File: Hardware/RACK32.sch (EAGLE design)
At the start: 95 parts, among them IC1 MCP9808-MSOP8, IC2 ESPWROOM32, IC3 LM358D, IC4 W5500-LQFP, IC5 CP2102N-A01-GQFN24, J1 SPI-LCD, J10 microSD, J11 IO, J2 I2CBR, J3 USB-C-16P-16P, J4 DC IN, J6 PWR_LED, Q1 FDN340P, Q2 MMDT3904, U1 HY931147C-RJ45

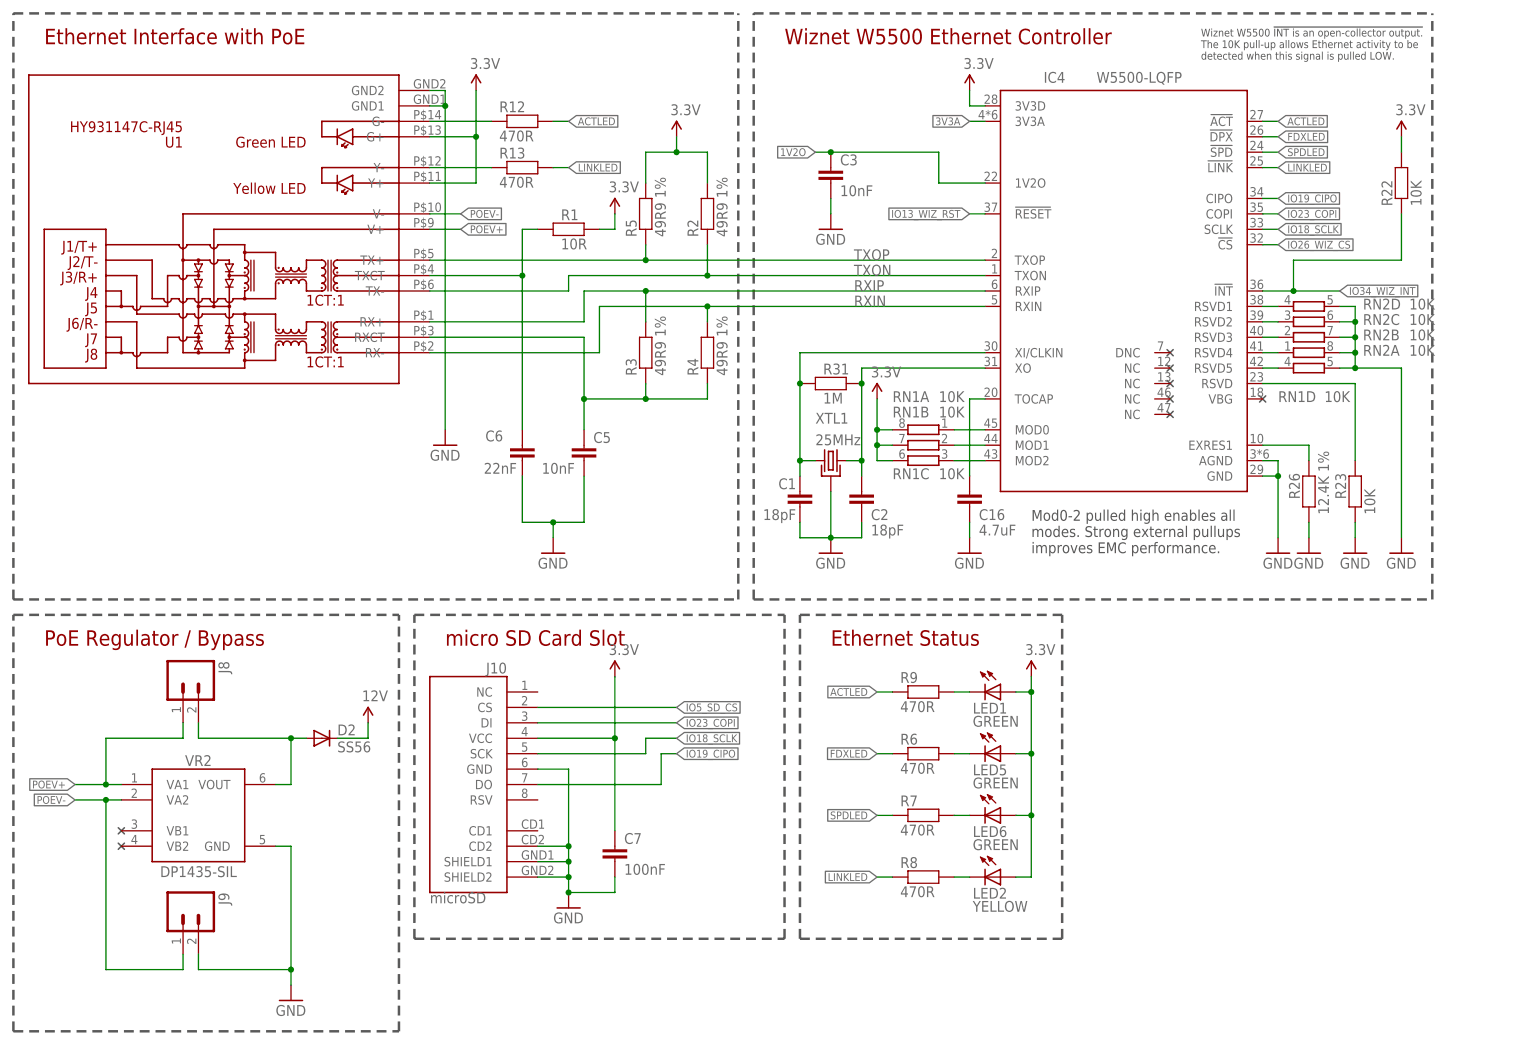
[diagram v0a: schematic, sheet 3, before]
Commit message: Changed PTC to 1206 size. Replaced power LED header.
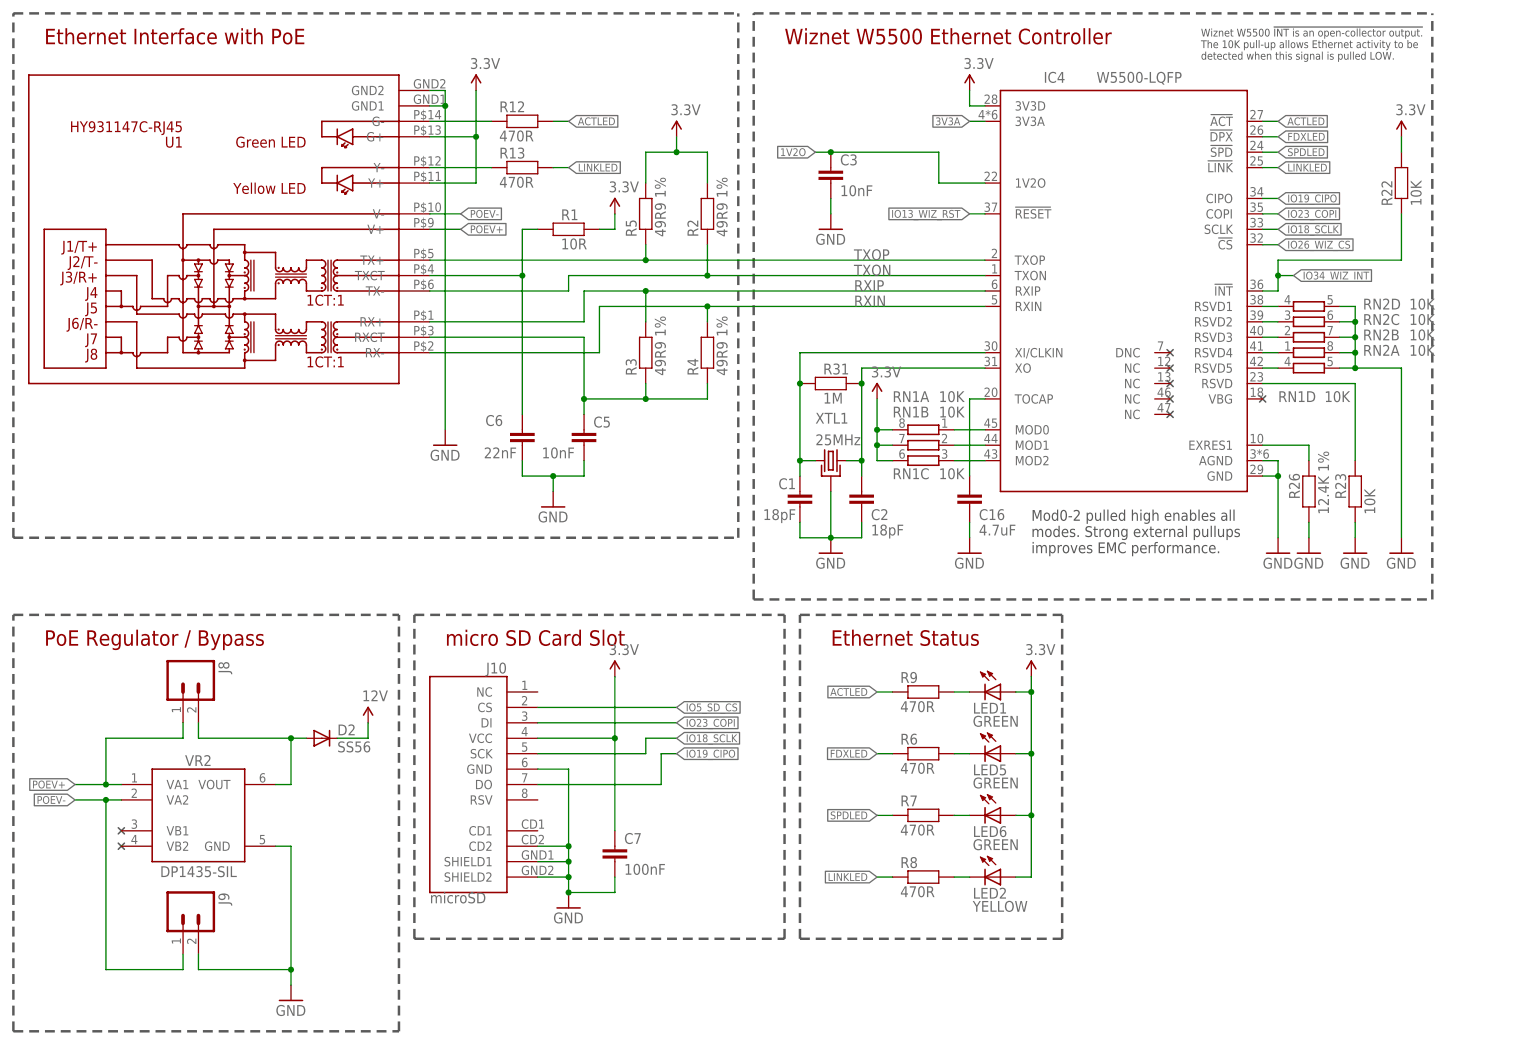
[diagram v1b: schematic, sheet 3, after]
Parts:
- F1: value 500mA 1812 PTC -> 500mA 1206 PTC; device SuperHouse-Fuses:PTC050-1812 -> SuperHouse-Fuses:PTC-1206
- J6: device SuperHouse-Connectors:M02-KF2510 -> SuperHouse-Connectors:M02-PIN
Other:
- note added: "ESP32 Pin Assignment: IO1: USB_TX IO2: TFT_DC IO3: USB_RX IO4: TFT_RST IO5: SD_CS IO13: WIZ_RST IO14: TFT_BLK IO16: RX2 IO17: TX2"
- note added: "IO18: SCLK IO19: CIPO IO21: SDA IO22: SCL IO23: COPI IO25: TFT_CS IO26: WIZ_CS IO32: SCL2 IO33: SDA2 IO34: WIZ_INT"
- note added: "OXRS Compatible. ID: OXRS-SHA-RACK32 https://oxrs.io/docs/hardware/controllers/rack32.html"
- note added: "Rack32"
- note added: "SKU: RACK32"
- note added: "V1.1 (2021-09-20)"
- note added: "www.superhouse.tv/rack32"
- note removed: "ESP32 Pin Assignment: IO1: USB_TX IO2: TFT_DC IO3: USB_RX IO4: TFT_RST IO5: SD_CS IO13: WIZ_RST IO14: TFT_BLK IO16: RX2 IO17: TX2 IO18: SCLK IO19: CIPO IO21: SDA IO22: SCL IO23: COPI IO25: TFT_CS IO26: WIZ_CS IO32: SCL2 IO33: SDA2 IO34: WIZ_INT"
- note removed: "SKU: URCESP32"
- note removed: "Universal Rack Controller ESP32"
- note removed: "V1.0 (2021-07-23)"
- note removed: "www.superhouse.tv/urcesp32"
- moved on the sheet: C5, C6

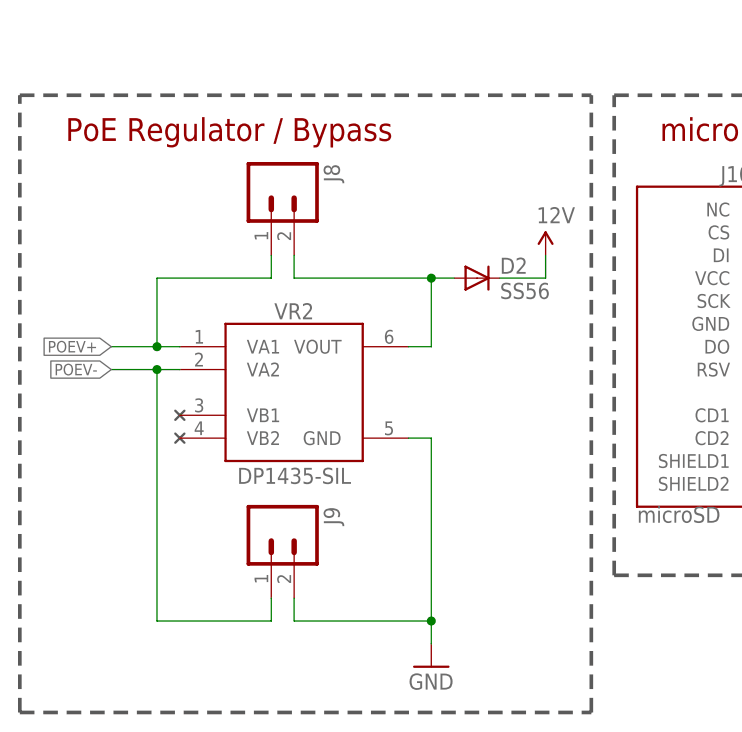
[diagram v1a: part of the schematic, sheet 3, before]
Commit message: Added backpower protection for PoE module.
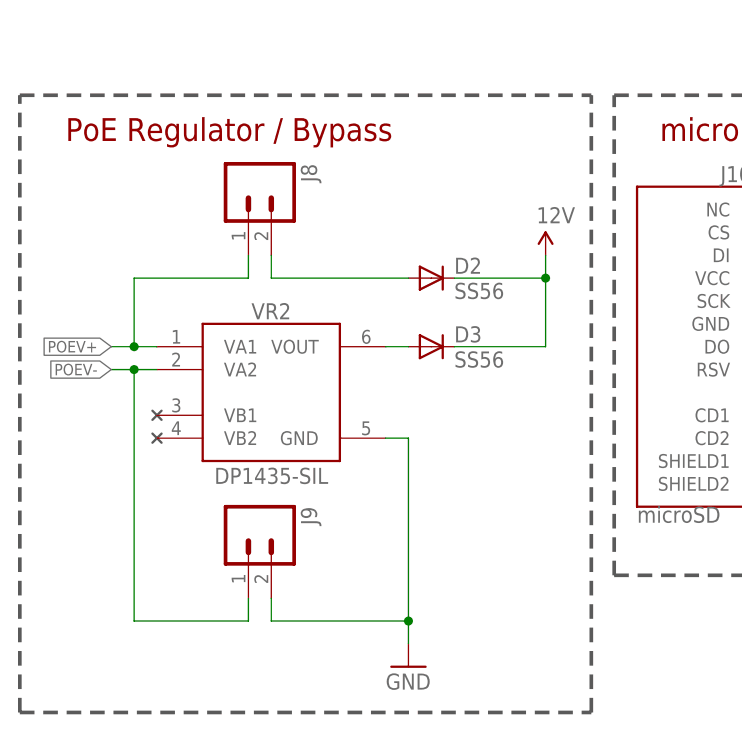
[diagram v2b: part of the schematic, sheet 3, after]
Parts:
- added D3: SS56, SuperHouse-Diodes:DIODESMA
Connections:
- new net N$13: D3.A, VR2.VOUT
- net 12V: now also D3.C
- net N$8: no longer VR2.VOUT
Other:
- moved on the sheet: D2, J8, J9, VR2
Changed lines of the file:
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@@
 <part name="P+24" library="SuperHouse-SupplySymbols" library_urn="urn:adsk.eagle:library:11790503" deviceset="3.3V" device=""/>
 <part name="GND10" library="SuperHouse-SupplySymbols" library_urn="urn:adsk.eagle:library:11790503" deviceset="GND" device=""/>
+<part name="D3" library="SuperHouse-Diodes" library_urn="urn:adsk.eagle:library:28961057" deviceset="DIODE" device="SMA" package3d_urn="urn:adsk.eagle:package:28961089/1" value="SS56"/>
 </parts>
 <sheets>
@@
 <attribute name="VALUE" x="105.664" y="148.336" size="1.778" layer="96"/>
 </instance>
-<instance part="D2" gate="G$1" x="58.42" y="58.42" smashed="yes">
-<attribute name="NAME" x="60.96" y="58.9026" size="1.778" layer="95"/>
-<attribute name="VALUE" x="60.96" y="56.1086" size="1.778" layer="96"/>
+<instance part="D2" gate="G$1" x="53.34" y="58.42" smashed="yes">
+<attribute name="NAME" x="55.88" y="58.9026" size="1.778" layer="95"/>
+<attribute name="VALUE" x="55.88" y="56.1086" size="1.778" layer="96"/>
 </instance>
 <instance part="RN1" gate="A" x="157.48" y="109.22" smashed="yes" rot="R180">
@@
 <attribute name="VALUE" x="153.67" y="32.258" size="1.778" layer="96"/>
 </instance>
-<instance part="J8" gate="G$1" x="35.56" y="68.58" smashed="yes" rot="R270">
-<attribute name="VALUE" x="30.48" y="71.12" size="1.778" layer="96" rot="R270"/>
-<attribute name="NAME" x="41.402" y="71.12" size="1.778" layer="95" rot="R270"/>
-</instance>
-<instance part="J9" gate="G$1" x="35.56" y="30.48" smashed="yes" rot="R270">
-<attribute name="VALUE" x="30.48" y="33.02" size="1.778" layer="96" rot="R270"/>
-<attribute name="NAME" x="41.402" y="33.02" size="1.778" layer="95" rot="R270"/>
-</instance>
-<instance part="GND3" gate="1" x="53.34" y="15.24" smashed="yes">
-<attribute name="VALUE" x="50.8" y="12.7" size="1.778" layer="96"/>
+<instance part="J8" gate="G$1" x="33.02" y="68.58" smashed="yes" rot="R270">
+<attribute name="VALUE" x="27.94" y="71.12" size="1.778" layer="96" rot="R270"/>
+<attribute name="NAME" x="38.862" y="71.12" size="1.778" layer="95" rot="R270"/>
+</instance>
+<instance part="J9" gate="G$1" x="33.02" y="30.48" smashed="yes" rot="R270">
+<attribute name="VALUE" x="27.94" y="33.02" size="1.778" layer="96" rot="R270"/>
+<attribute name="NAME" x="38.862" y="33.02" size="1.778" layer="95" rot="R270"/>
+</instance>
+<instance part="GND3" gate="1" x="50.8" y="15.24" smashed="yes">
+<attribute name="VALUE" x="48.26" y="12.7" size="1.778" layer="96"/>
 </instance>
 <instance part="P+1" gate="G$1" x="66.04" y="60.96" smashed="yes">
 <attribute name="VALUE" x="65.024" y="64.516" size="1.778" layer="96"/>
 </instance>
-<instance part="VR2" gate="G$1" x="38.1" y="45.72" smashed="yes">
-<attribute name="NAME" x="38.1" y="53.848" size="1.778" layer="95" align="bottom-center"/>
-<attribute name="VALUE" x="38.1" y="35.56" size="1.778" layer="96" align="bottom-center"/>
-</instance>
-<instance part="NC2" gate="G$1" x="25.4" y="43.18" smashed="yes"/>
-<instance part="NC3" gate="G$1" x="25.4" y="40.64" smashed="yes"/>
+<instance part="VR2" gate="G$1" x="35.56" y="45.72" smashed="yes">
+<attribute name="NAME" x="35.56" y="53.848" size="1.778" layer="95" align="bottom-center"/>
+<attribute name="VALUE" x="35.56" y="35.56" size="1.778" layer="96" align="bottom-center"/>
+</instance>
+<instance part="NC2" gate="G$1" x="22.86" y="43.18" smashed="yes"/>
+<instance part="NC3" gate="G$1" x="22.86" y="40.64" smashed="yes"/>
+<instance part="D3" gate="G$1" x="53.34" y="50.8" smashed="yes">
+<attribute name="NAME" x="55.88" y="51.2826" size="1.778" layer="95"/>
+<attribute name="VALUE" x="55.88" y="48.4886" size="1.778" layer="96"/>
+</instance>
 </instances>
 <busses>
@@
 <segment>
 <pinref part="GND3" gate="1" pin="GND"/>
-<wire x1="53.34" y1="40.64" x2="53.34" y2="20.32" width="0.1524" layer="91"/>
+<wire x1="50.8" y1="40.64" x2="50.8" y2="20.32" width="0.1524" layer="91"/>
 <pinref part="J9" gate="G$1" pin="2"/>
-<wire x1="53.34" y1="20.32" x2="53.34" y2="17.78" width="0.1524" layer="91"/>
-<wire x1="38.1" y1="22.86" x2="38.1" y2="20.32" width="0.1524" layer="91"/>
-<wire x1="38.1" y1="20.32" x2="53.34" y2="20.32" width="0.1524" layer="91"/>
-<junction x="53.34" y="20.32"/>
+<wire x1="50.8" y1="20.32" x2="50.8" y2="17.78" width="0.1524" layer="91"/>
+<wire x1="35.56" y1="22.86" x2="35.56" y2="20.32" width="0.1524" layer="91"/>
+<wire x1="35.56" y1="20.32" x2="50.8" y2="20.32" width="0.1524" layer="91"/>
+<junction x="50.8" y="20.32"/>
 <pinref part="VR2" gate="G$1" pin="GND"/>
-<wire x1="50.8" y1="40.64" x2="53.34" y2="40.64" width="0.1524" layer="91"/>
+<wire x1="48.26" y1="40.64" x2="50.8" y2="40.64" width="0.1524" layer="91"/>
 </segment>
 </net>
@@
 </segment>
 <segment>
-<wire x1="22.86" y1="50.8" x2="17.78" y2="50.8" width="0.1524" layer="91"/>
-<wire x1="22.86" y1="50.8" x2="22.86" y2="58.42" width="0.1524" layer="91"/>
-<wire x1="22.86" y1="58.42" x2="35.56" y2="58.42" width="0.1524" layer="91"/>
+<wire x1="20.32" y1="50.8" x2="17.78" y2="50.8" width="0.1524" layer="91"/>
+<wire x1="20.32" y1="50.8" x2="20.32" y2="58.42" width="0.1524" layer="91"/>
+<wire x1="20.32" y1="58.42" x2="33.02" y2="58.42" width="0.1524" layer="91"/>
 <pinref part="J8" gate="G$1" pin="1"/>
-<wire x1="35.56" y1="58.42" x2="35.56" y2="60.96" width="0.1524" layer="91"/>
+<wire x1="33.02" y1="58.42" x2="33.02" y2="60.96" width="0.1524" layer="91"/>
 <label x="17.78" y="50.8" size="1.27" layer="95" rot="R180" xref="yes"/>
 <pinref part="VR2" gate="G$1" pin="VA1"/>
-<wire x1="22.86" y1="50.8" x2="25.4" y2="50.8" width="0.1524" layer="91"/>
-<junction x="22.86" y="50.8"/>
+<wire x1="20.32" y1="50.8" x2="22.86" y2="50.8" width="0.1524" layer="91"/>
+<junction x="20.32" y="50.8"/>
 </segment>
 </net>
@@
 </segment>
 <segment>
-<wire x1="22.86" y1="48.26" x2="17.78" y2="48.26" width="0.1524" layer="91"/>
-<wire x1="22.86" y1="48.26" x2="22.86" y2="20.32" width="0.1524" layer="91"/>
-<wire x1="22.86" y1="20.32" x2="35.56" y2="20.32" width="0.1524" layer="91"/>
+<wire x1="20.32" y1="48.26" x2="17.78" y2="48.26" width="0.1524" layer="91"/>
+<wire x1="20.32" y1="48.26" x2="20.32" y2="20.32" width="0.1524" layer="91"/>
+<wire x1="20.32" y1="20.32" x2="33.02" y2="20.32" width="0.1524" layer="91"/>
 <pinref part="J9" gate="G$1" pin="1"/>
-<wire x1="35.56" y1="20.32" x2="35.56" y2="22.86" width="0.1524" layer="91"/>
+<wire x1="33.02" y1="20.32" x2="33.02" y2="22.86" width="0.1524" layer="91"/>
 <label x="17.78" y="48.26" size="1.27" layer="95" rot="R180" xref="yes"/>
 <pinref part="VR2" gate="G$1" pin="VA2"/>
-<wire x1="22.86" y1="48.26" x2="25.4" y2="48.26" width="0.1524" layer="91"/>
-<junction x="22.86" y="48.26"/>
+<wire x1="20.32" y1="48.26" x2="22.86" y2="48.26" width="0.1524" layer="91"/>
+<junction x="20.32" y="48.26"/>
 </segment>
 </net>
@@
 <segment>
 <pinref part="J8" gate="G$1" pin="2"/>
-<wire x1="38.1" y1="60.96" x2="38.1" y2="58.42" width="0.1524" layer="91"/>
-<wire x1="38.1" y1="58.42" x2="53.34" y2="58.42" width="0.1524" layer="91"/>
-<pinref part="VR2" gate="G$1" pin="VOUT"/>
-<wire x1="50.8" y1="50.8" x2="53.34" y2="50.8" width="0.1524" layer="91"/>
-<wire x1="53.34" y1="50.8" x2="53.34" y2="58.42" width="0.1524" layer="91"/>
+<wire x1="35.56" y1="60.96" x2="35.56" y2="58.42" width="0.1524" layer="91"/>
+<wire x1="35.56" y1="58.42" x2="50.8" y2="58.42" width="0.1524" layer="91"/>
 <pinref part="D2" gate="G$1" pin="A"/>
-<wire x1="55.88" y1="58.42" x2="53.34" y2="58.42" width="0.1524" layer="91"/>
-<junction x="53.34" y="58.42"/>
 </segment>
 </net>
@@
 <segment>
 <pinref part="D2" gate="G$1" pin="C"/>
-<wire x1="60.96" y1="58.42" x2="66.04" y2="58.42" width="0.1524" layer="91"/>
+<wire x1="55.88" y1="58.42" x2="66.04" y2="58.42" width="0.1524" layer="91"/>
 <pinref part="P+1" gate="G$1" pin="12V"/>
 <wire x1="66.04" y1="58.42" x2="66.04" y2="60.96" width="0.1524" layer="91"/>
+<pinref part="D3" gate="G$1" pin="C"/>
+<wire x1="55.88" y1="50.8" x2="66.04" y2="50.8" width="0.1524" layer="91"/>
+<wire x1="66.04" y1="50.8" x2="66.04" y2="58.42" width="0.1524" layer="91"/>
+<junction x="66.04" y="58.42"/>
 </segment>
 </net>
@@
 </segment>
 </net>
+<net name="N$13" class="0">
+<segment>
+<pinref part="VR2" gate="G$1" pin="VOUT"/>
+<pinref part="D3" gate="G$1" pin="A"/>
+<wire x1="48.26" y1="50.8" x2="50.8" y2="50.8" width="0.1524" layer="91"/>
+</segment>
+</net>

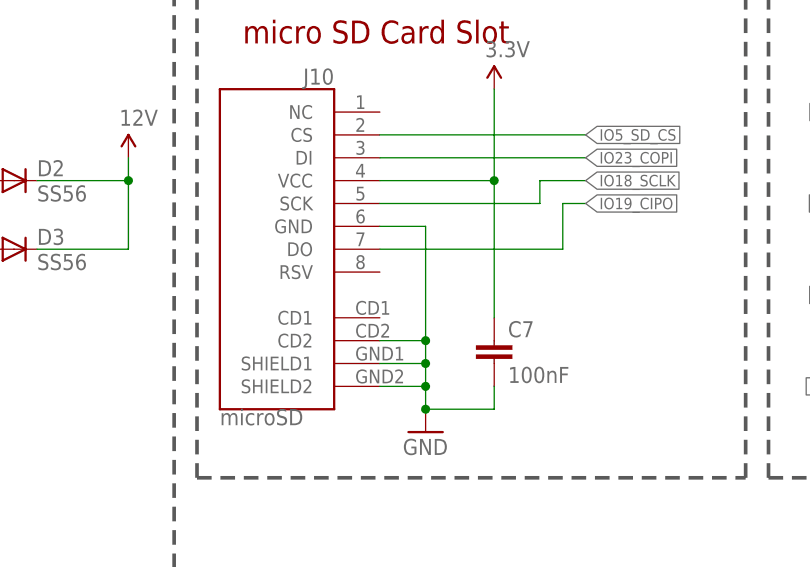
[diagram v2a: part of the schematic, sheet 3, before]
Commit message: Added link to OXRS.io on the silkscreen. Connected second SD card detect pad to GND for improved mechanical strength.
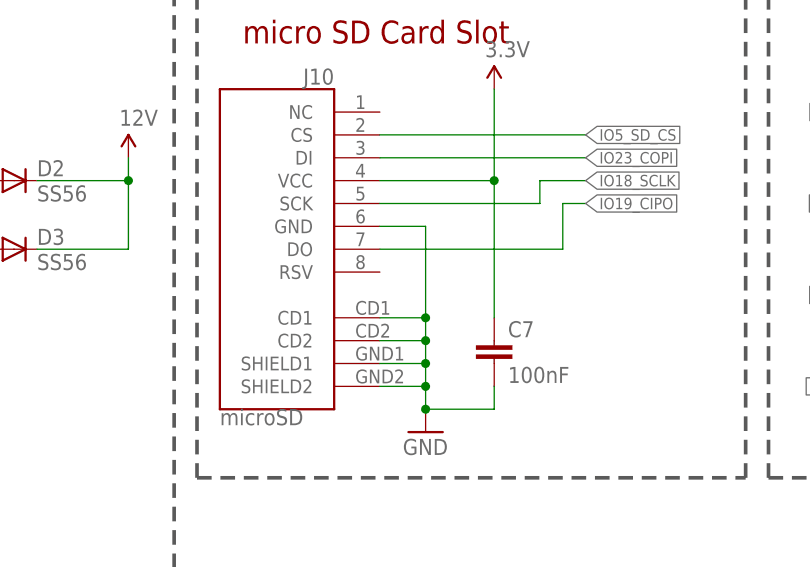
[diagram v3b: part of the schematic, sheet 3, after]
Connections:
- net GND: now also J10.CD1
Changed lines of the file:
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@@
 <wire x1="93.98" y1="35.56" x2="99.06" y2="35.56" width="0.1524" layer="91"/>
 <wire x1="93.98" y1="53.34" x2="99.06" y2="53.34" width="0.1524" layer="91"/>
-<wire x1="99.06" y1="53.34" x2="99.06" y2="40.64" width="0.1524" layer="91"/>
+<wire x1="99.06" y1="53.34" x2="99.06" y2="43.18" width="0.1524" layer="91"/>
+<wire x1="99.06" y1="43.18" x2="99.06" y2="40.64" width="0.1524" layer="91"/>
 <wire x1="99.06" y1="33.02" x2="99.06" y2="35.56" width="0.1524" layer="91"/>
 <junction x="99.06" y="38.1"/>
@@
 <pinref part="C7" gate="G$1" pin="2"/>
 <wire x1="99.06" y1="33.02" x2="106.68" y2="33.02" width="0.1524" layer="91"/>
+<pinref part="J10" gate="G$1" pin="CD1"/>
+<wire x1="93.98" y1="43.18" x2="99.06" y2="43.18" width="0.1524" layer="91"/>
+<junction x="99.06" y="43.18"/>
 </segment>
 <segment>
